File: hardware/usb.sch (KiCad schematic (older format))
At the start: 33 parts, among them J2 USB_B_Micro, U14 FT2232H, U31 93LCxxB, Y1 12MHz

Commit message: Improved documentation and parts of the schematic.
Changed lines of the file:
@@
 U 1 1 583B312F
 P 4400 3350
-F 0 "R80" V 4300 3350 50  0000 C CNN
-F 1 "0" V 4400 3350 50  0000 C CNN
+F 0 "R80" V 4193 3350 50  0000 C CNN
+F 1 "0" V 4284 3350 50  0000 C CNN
 F 2 "Resistor_SMD:R_0402_1005Metric" V 4330 3350 30  0001 C CNN
 F 3 "" H 4400 3350 30  0000 C CNN
@@
 U 1 1 583B315C
 P 4400 3450
-F 0 "R81" V 4480 3450 50  0000 C CNN
-F 1 "0" V 4400 3450 50  0000 C CNN
+F 0 "R81" V 4500 3450 50  0000 C CNN
+F 1 "0" V 4600 3450 50  0000 C CNN
 F 2 "Resistor_SMD:R_0402_1005Metric" V 4330 3450 30  0001 C CNN
 F 3 "" H 4400 3450 30  0000 C CNN
@@
 U 1 1 583B5C84
 P 8000 4150
-F 0 "R84" V 8080 4150 50  0000 C CNN
-F 1 "33" V 8000 4150 50  0000 C CNN
+F 0 "R84" V 7793 4150 50  0000 C CNN
+F 1 "33" V 7884 4150 50  0000 C CNN
 F 2 "Resistor_SMD:R_0402_1005Metric" V 7930 4150 30  0001 C CNN
 F 3 "" H 8000 4150 30  0000 C CNN
@@
 U 1 1 583B5CC5
 P 8400 4250
-F 0 "R88" V 8480 4250 50  0000 C CNN
-F 1 "33" V 8400 4250 50  0000 C CNN
+F 0 "R88" V 8200 4250 50  0000 C CNN
+F 1 "33" V 8300 4250 50  0000 C CNN
 F 2 "Resistor_SMD:R_0402_1005Metric" V 8330 4250 30  0001 C CNN
 F 3 "" H 8400 4250 30  0000 C CNN
@@
 U 1 1 583B63A8
 P 8000 4450
-F 0 "R85" V 8080 4450 50  0000 C CNN
-F 1 "33" V 8000 4450 50  0000 C CNN
+F 0 "R85" V 8115 4450 50  0000 C CNN
+F 1 "33" V 8206 4450 50  0000 C CNN
 F 2 "Resistor_SMD:R_0402_1005Metric" V 7930 4450 30  0001 C CNN
 F 3 "" H 8000 4450 30  0000 C CNN
@@
 U 1 1 596BF8E7
 P 4850 3850
-F 0 "R72" V 4930 3850 50  0000 C CNN
-F 1 "1k" V 4850 3850 50  0000 C CNN
+F 0 "R72" V 4965 3850 50  0000 C CNN
+F 1 "1k" V 5056 3850 50  0000 C CNN
 F 2 "Resistor_SMD:R_0402_1005Metric" V 4780 3850 30  0001 C CNN
 F 3 "" H 4850 3850 30  0000 C CNN

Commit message: Changed components to official libs.
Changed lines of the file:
@@
 U 1 1 596C00A3
 P 4250 3900
-F 0 "R71" V 4330 3900 50  0000 C CNN
-F 1 "12k" V 4250 3900 50  0000 C CNN
+F 0 "R71" H 4181 3946 50  0000 R CNN
+F 1 "12k" H 4181 3855 50  0000 R CNN
 F 2 "Resistor_SMD:R_0402_1005Metric" V 4180 3900 30  0001 C CNN
 F 3 "" H 4250 3900 30  0000 C CNN

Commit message: Finished design, began routing.
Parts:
- R26: renamed from R82; MFN ERJ-2GEJ472X -> ERJ-2GEJ472X
- Y1: footprint Crystal:Crystal_SMD_Abracon_ABM10-4Pin_2.5x2.0mm -> fmcw:ABM10; symbol Device:Crystal -> Device:Crystal_GND24
- renumbered C207 to C59, C208 to C60, C209 to C61, C152 to C62, C153 to C63, C154 to C64, C210 to C65, C155 to C66, C156 to C67, C157 to C68, C211 to C69, C212 to C70, C158 to C71, C159 to C72, C160 to C73, C161 to C74, FB14 to FB3, FB12 to FB4, R73 to R17, R79 to R18, R71 to R19, R80 to R20, R81 to R21, R72 to R22, R84 to R23, R85 to R24, R88 to R25, R83 to R27, U31 to U8, U14 to U9
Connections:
- wire segments 134 -> 139
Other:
- moved on the sheet: C62, C63, C64, R26

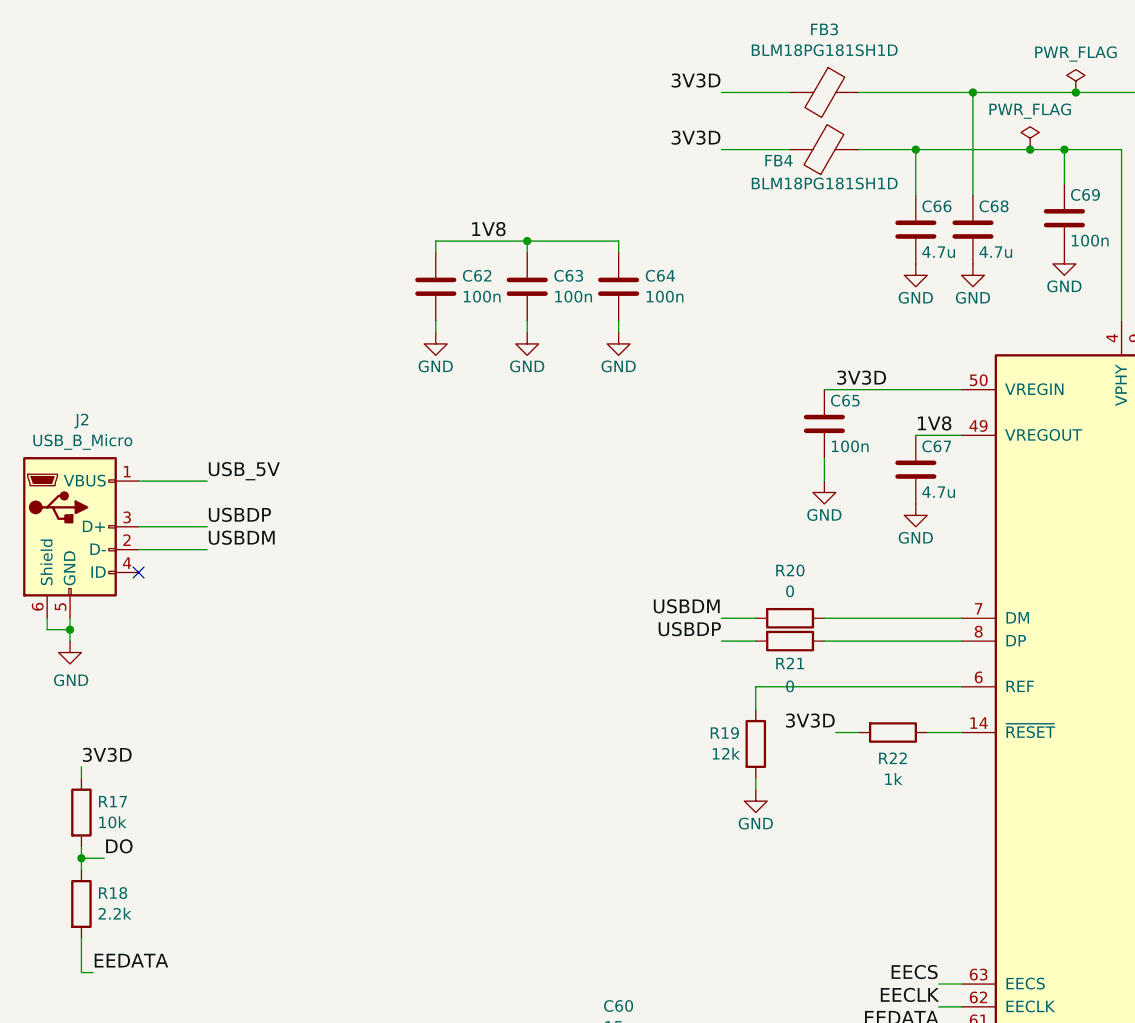
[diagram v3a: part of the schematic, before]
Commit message: Completed clock placement and routing.
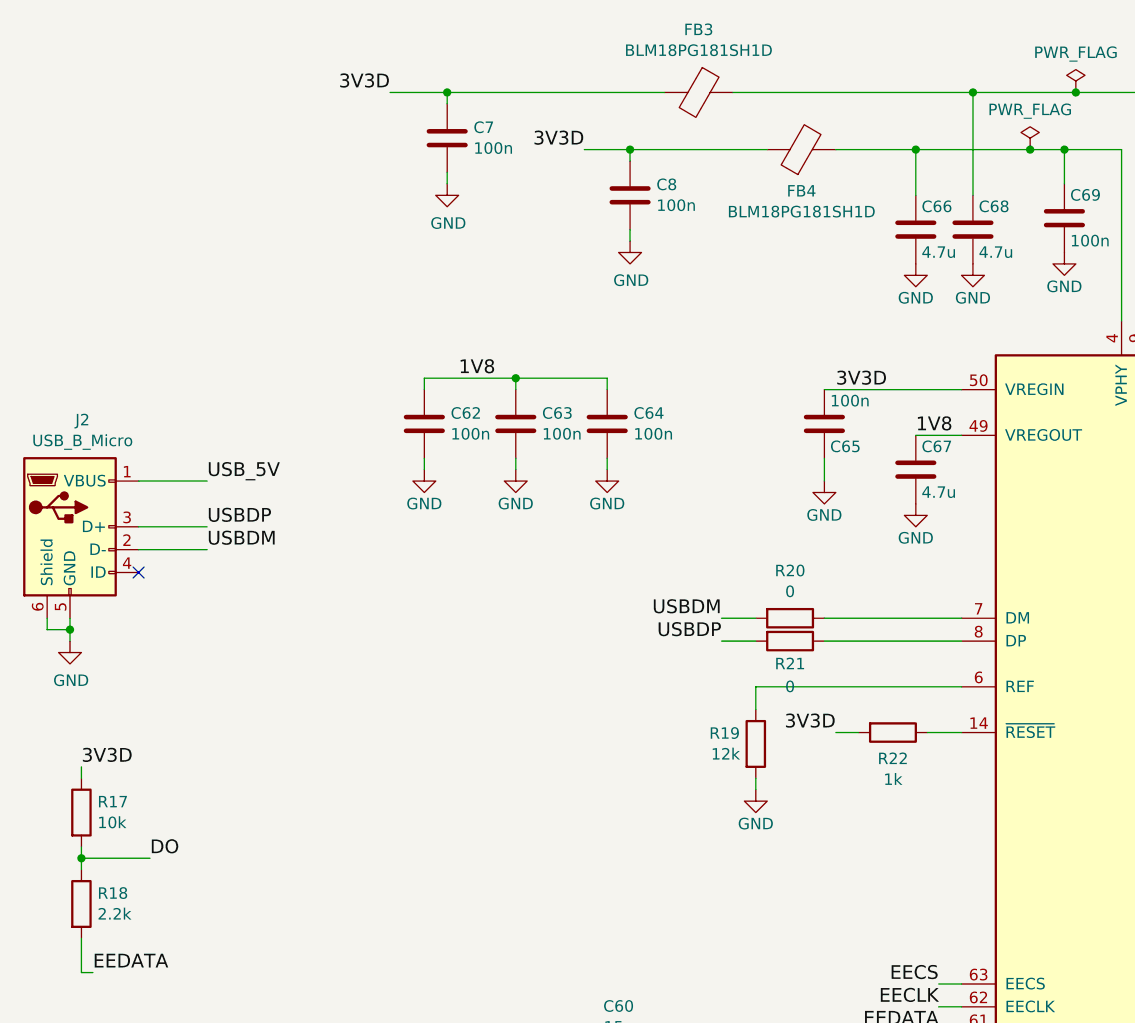
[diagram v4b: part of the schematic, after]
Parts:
- added C7, C8: 100n, Capacitor_SMD:C_0402_1005Metric, symbol Device:C
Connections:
- net 3V3D: now also C65.2, C7.1, C8.1; no longer C65.1
- net GND: now also C65.1, C7.2, C8.2; no longer C65.2
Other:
- moved on the sheet: C62, C63, C64, FB3, FB4
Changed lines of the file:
@@
 F 4 "CL05B104KO5NNNC" H 0   0   50  0001 C CNN "MFN"
 	1    4550 2500
-	1    0    0    -1
+	1    0    0    1
 $EndComp
 $Comp
@@
 	1    0    0    -1
 $EndComp
-Text Label 1400 4400 0    60   ~ 0
+Text Label 1600 4400 0    60   ~ 0
 DO
 Text Label 1350 4900 0    60   ~ 0
@@
 L Device:Ferrite_Bead FB4
 U 1 1 5865C0D7
-P 4550 1300
-F 0 "FB4" V 4500 1500 50  0000 C CNN
-F 1 "BLM18PG181SH1D" V 4400 1300 50  0000 C CNN
-F 2 "Inductor_SMD:L_0603_1608Metric" H 4550 1300 60  0001 C CNN
-F 3 "" H 4550 1300 60  0000 C CNN
-F 4 "BLM18PG181SH1D" H 0   0   50  0001 C CNN "MFN"
-	1    4550 1300
+P 4450 1300
+F 0 "FB4" V 4268 1300 50  0000 C CNN
+F 1 "BLM18PG181SH1D" V 4177 1300 50  0000 C CNN
+F 2 "Inductor_SMD:L_0603_1608Metric" H 4450 1300 60  0001 C CNN
+F 3 "" H 4450 1300 60  0000 C CNN
+F 4 "BLM18PG181SH1D" H -100 0   50  0001 C CNN "MFN"
+	1    4450 1300
 	0    -1   -1   0
 $EndComp
@@
 L Device:Ferrite_Bead FB3
 U 1 1 596BB650
-P 4550 1050
-F 0 "FB3" V 4276 1050 50  0000 C CNN
-F 1 "BLM18PG181SH1D" V 4367 1050 50  0000 C CNN
-F 2 "Inductor_SMD:L_0603_1608Metric" H 4550 1050 60  0001 C CNN
-F 3 "" H 4550 1050 60  0000 C CNN
-F 4 "BLM18PG181SH1D" H 0   0   50  0001 C CNN "MFN"
-	1    4550 1050
+P 4000 1050
+F 0 "FB3" V 3726 1050 50  0000 C CNN
+F 1 "BLM18PG181SH1D" V 3817 1050 50  0000 C CNN
+F 2 "Inductor_SMD:L_0603_1608Metric" H 4000 1050 60  0001 C CNN
+F 3 "" H 4000 1050 60  0000 C CNN
+F 4 "BLM18PG181SH1D" H -550 0   50  0001 C CNN "MFN"
+	1    4000 1050
 	0    1    1    0
 $EndComp
@@
 	1300 4900 1350 4900
 Wire Wire Line
-	1400 4400 1300 4400
+	1600 4400 1300 4400
 Connection ~ 1300 4400
 Wire Wire Line
@@
 	1    0    0    -1
 $EndComp
-Text Label 4100 1050 2    60   ~ 0
+Text Label 2650 1050 2    60   ~ 0
 3V3D
-Text Label 4100 1300 2    60   ~ 0
+Text Label 3500 1300 2    60   ~ 0
 3V3D
 $Comp
@@
 L Device:C C63
 U 1 1 596C4AA8
-P 3250 1900
-F 0 "C63" H 3365 1946 50  0000 L CNN
-F 1 "100n" H 3365 1855 50  0000 L CNN
-F 2 "Capacitor_SMD:C_0402_1005Metric" H 3288 1750 30  0001 C CNN
-F 3 "" H 3250 1900 60  0000 C CNN
-F 4 "CL05B104KO5NNNC" H -700 0   50  0001 C CNN "MFN"
-	1    3250 1900
+P 3200 2500
+F 0 "C63" H 3315 2546 50  0000 L CNN
+F 1 "100n" H 3315 2455 50  0000 L CNN
+F 2 "Capacitor_SMD:C_0402_1005Metric" H 3238 2350 30  0001 C CNN
+F 3 "" H 3200 2500 60  0000 C CNN
+F 4 "CL05B104KO5NNNC" H -750 600 50  0001 C CNN "MFN"
+	1    3200 2500
 	1    0    0    -1
 $EndComp
@@
 L Device:C C64
 U 1 1 596C4AFE
-P 3650 1900
-F 0 "C64" H 3765 1946 50  0000 L CNN
-F 1 "100n" H 3765 1855 50  0000 L CNN
-F 2 "Capacitor_SMD:C_0402_1005Metric" H 3688 1750 30  0001 C CNN
-F 3 "" H 3650 1900 60  0000 C CNN
-F 4 "CL05B104KO5NNNC" H -500 0   50  0001 C CNN "MFN"
-	1    3650 1900
+P 3600 2500
+F 0 "C64" H 3715 2546 50  0000 L CNN
+F 1 "100n" H 3715 2455 50  0000 L CNN
+F 2 "Capacitor_SMD:C_0402_1005Metric" H 3638 2350 30  0001 C CNN
+F 3 "" H 3600 2500 60  0000 C CNN
+F 4 "CL05B104KO5NNNC" H -550 600 50  0001 C CNN "MFN"
+	1    3600 2500
 	1    0    0    -1
 $EndComp
@@
 L power:GND #PWR055
 U 1 1 596C4CA2
-P 3650 2100
-F 0 "#PWR055" H 3650 1850 50  0001 C CNN
-F 1 "GND" H 3650 1950 50  0000 C CNN
-F 2 "" H 3650 2100 60  0000 C CNN
-F 3 "" H 3650 2100 60  0000 C CNN
-	1    3650 2100
+P 3600 2700
+F 0 "#PWR055" H 3600 2450 50  0001 C CNN
+F 1 "GND" H 3600 2550 50  0000 C CNN
+F 2 "" H 3600 2700 60  0000 C CNN
+F 3 "" H 3600 2700 60  0000 C CNN
+	1    3600 2700
 	1    0    0    -1
 $EndComp
@@
 L power:GND #PWR054
 U 1 1 596C4CF6
-P 3250 2100
-F 0 "#PWR054" H 3250 1850 50  0001 C CNN
-F 1 "GND" H 3250 1950 50  0000 C CNN
-F 2 "" H 3250 2100 60  0000 C CNN
-F 3 "" H 3250 2100 60  0000 C CNN
-	1    3250 2100
+P 3200 2700
+F 0 "#PWR054" H 3200 2450 50  0001 C CNN
+F 1 "GND" H 3200 2550 50  0000 C CNN
+F 2 "" H 3200 2700 60  0000 C CNN
+F 3 "" H 3200 2700 60  0000 C CNN
+	1    3200 2700
 	1    0    0    -1
 $EndComp
@@
 L power:GND #PWR053
 U 1 1 596C4D43
-P 2850 2100
-F 0 "#PWR053" H 2850 1850 50  0001 C CNN
-F 1 "GND" H 2850 1950 50  0000 C CNN
-F 2 "" H 2850 2100 60  0000 C CNN
-F 3 "" H 2850 2100 60  0000 C CNN
-	1    2850 2100
-	1    0    0    -1
-$EndComp
-Wire Wire Line
-	3250 1700 3250 1750
-Wire Wire Line
-	3650 1700 3650 1750
-Text Label 3000 1700 0    60   ~ 0
+P 2800 2700
+F 0 "#PWR053" H 2800 2450 50  0001 C CNN
+F 1 "GND" H 2800 2550 50  0000 C CNN
+F 2 "" H 2800 2700 60  0000 C CNN
+F 3 "" H 2800 2700 60  0000 C CNN
+	1    2800 2700
+	1    0    0    -1
+$EndComp
+Wire Wire Line
+	3200 2300 3200 2350
+Wire Wire Line
+	3600 2300 3600 2350
+Text Label 2950 2300 0    60   ~ 0
 1V8
 Wire Wire Line
@@
 	6250 1950 6350 1950
 Wire Wire Line
-	3250 1700 3650 1700
+	3200 2300 3600 2300
 $Comp
 L Interface_USB:FT2232H U9
@@
 $EndComp
 Wire Wire Line
-	4700 1300 4950 1300
-Wire Wire Line
-	4100 1300 4400 1300
-Wire Wire Line
-	4100 1050 4400 1050
-Wire Wire Line
-	4700 1050 5200 1050
+	4600 1300 4950 1300
+Wire Wire Line
+	2650 1050 2900 1050
+Wire Wire Line
+	4150 1050 5200 1050
 Wire Wire Line
 	8600 5300 8600 5400
@@
 	6650 1050 7150 1050
 Wire Wire Line
-	2850 2100 2850 2050
+	2800 2700 2800 2650
 $Comp
 L Device:C C62
 U 1 1 596C4A23
-P 2850 1900
-F 0 "C62" H 2965 1946 50  0000 L CNN
-F 1 "100n" H 2965 1855 50  0000 L CNN
-F 2 "Capacitor_SMD:C_0402_1005Metric" H 2888 1750 30  0001 C CNN
-F 3 "" H 2850 1900 60  0000 C CNN
-F 4 "CL05B104KO5NNNC" H -900 0   50  0001 C CNN "MFN"
-	1    2850 1900
-	1    0    0    -1
-$EndComp
-Connection ~ 3250 1700
-Wire Wire Line
-	2850 1700 2850 1750
-Wire Wire Line
-	2850 1700 3250 1700
-Wire Wire Line
-	3250 2100 3250 2050
-Wire Wire Line
-	3650 2100 3650 2050
+P 2800 2500
+F 0 "C62" H 2915 2546 50  0000 L CNN
+F 1 "100n" H 2915 2455 50  0000 L CNN
+F 2 "Capacitor_SMD:C_0402_1005Metric" H 2838 2350 30  0001 C CNN
+F 3 "" H 2800 2500 60  0000 C CNN
+F 4 "CL05B104KO5NNNC" H -950 600 50  0001 C CNN "MFN"
+	1    2800 2500
+	1    0    0    -1
+$EndComp
+Connection ~ 3200 2300
+Wire Wire Line
+	2800 2300 2800 2350
+Wire Wire Line
+	2800 2300 3200 2300
+Wire Wire Line
+	3200 2700 3200 2650
+Wire Wire Line
+	3600 2700 3600 2650
 Wire Wire Line
 	4250 4100 4250 4050
@@
 NoConn ~ 3600 5650
 NoConn ~ 4000 5650
+$Comp
+L Device:C C8
+U 1 1 5C794EE9
+P 3700 1500
+F 0 "C8" H 3815 1546 50  0000 L CNN
+F 1 "100n" H 3815 1455 50  0000 L CNN
+F 2 "Capacitor_SMD:C_0402_1005Metric" H 3738 1350 30  0001 C CNN
+F 3 "" H 3700 1500 60  0000 C CNN
+F 4 "CL05B104KO5NNNC" H -1900 -100 50  0001 C CNN "MFN"
+	1    3700 1500
+	1    0    0    -1
+$EndComp
+Wire Wire Line
+	3500 1300 3700 1300
+$Comp
+L Device:C C7
+U 1 1 5C7A4A00
+P 2900 1250
+F 0 "C7" H 3015 1296 50  0000 L CNN
+F 1 "100n" H 3015 1205 50  0000 L CNN
+F 2 "Capacitor_SMD:C_0402_1005Metric" H 2938 1100 30  0001 C CNN
+F 3 "" H 2900 1250 60  0000 C CNN
+F 4 "CL05B104KO5NNNC" H -2700 -350 50  0001 C CNN "MFN"
+	1    2900 1250
+	1    0    0    -1
+$EndComp
+$Comp
+L power:GND #PWR011
+U 1 1 5C7A52FB
+P 2900 1450
+F 0 "#PWR011" H 2900 1200 50  0001 C CNN
+F 1 "GND" H 2905 1277 50  0000 C CNN
+F 2 "" H 2900 1450 50  0001 C CNN
+F 3 "" H 2900 1450 50  0001 C CNN
+	1    2900 1450
+	1    0    0    -1
+$EndComp
+Wire Wire Line
+	2900 1450 2900 1400
+Wire Wire Line
+	2900 1050 2900 1100
+Connection ~ 2900 1050
+Wire Wire Line
+	2900 1050 3850 1050
+Wire Wire Line
+	3700 1350 3700 1300
+Connection ~ 3700 1300
+Wire Wire Line
+	3700 1300 4300 1300
+$Comp
+L power:GND #PWR079
+U 1 1 5C7B858F
+P 3700 1700
+F 0 "#PWR079" H 3700 1450 50  0001 C CNN
+F 1 "GND" H 3705 1527 50  0000 C CNN
+F 2 "" H 3700 1700 50  0001 C CNN
+F 3 "" H 3700 1700 50  0001 C CNN
+	1    3700 1700
+	1    0    0    -1
+$EndComp
+Wire Wire Line
+	3700 1700 3700 1650
 $EndSCHEMATC

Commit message: Improve PCB.
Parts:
- removed U8: 93LCxxB, Package_SO:SOIC-8_3.9x4.9mm_P1.27mm, symbol Memory_EEPROM:93LCxxB
- added R3, R82: 10k, Resistor_SMD:R_0402_1005Metric, symbol Device:R
- added U8: 93LCxxBxxOT, Package_TO_SOT_SMD:SOT-23-6, symbol Memory_EEPROM:93LCxxBxxOT
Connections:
- net 3V3D: now also R3.1, R82.1, U8.6 (VCC)
- net DO: now also U8.1 (DO)
- net EECLK: now also R3.2, U8.4 (CLK)
- net EECS: now also R82.2, U8.5 (CS)
- net EEDATA: now also U8.3 (DI)
- net GND: now also U8.2 (GND)
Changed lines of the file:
@@
 Title "FMCW"
 Date ""
-Rev "v2.0"
+Rev "v2.0c"
 Comp ""
 Comment1 ""
@@
 	1    0    0    -1
 $EndComp
-Text Label 2950 6950 2    60   ~ 0
+Text Label 2950 7050 2    60   ~ 0
 EECS
 Text Label 4000 6950 0    60   ~ 0
@@
 	1300 4350 1300 4400
 Wire Wire Line
-	2950 6950 3100 6950
+	2950 7050 3100 7050
 Wire Wire Line
 	4000 6950 3900 6950
@@
 	5100 6050 5100 6550
 Wire Wire Line
-	5150 4950 5050 4950
-Wire Wire Line
-	5150 5050 5050 5050
+	5150 4950 4950 4950
+Wire Wire Line
+	5150 5050 4300 5050
 Wire Wire Line
 	5150 5150 5050 5150
-Text Label 5050 4950 2    60   ~ 0
+Text Label 4800 4950 2    60   ~ 0
 EECS
-Text Label 5050 5050 2    60   ~ 0
+Text Label 4150 5050 2    60   ~ 0
 EECLK
 Text Label 5050 5150 2    60   ~ 0
@@
 Wire Wire Line
 	7550 5750 8600 5750
-$Comp
-L Memory_EEPROM:93LCxxB U8
-U 1 1 6321F24D
-P 3500 7050
-F 0 "U8" H 3750 6800 50  0000 C CNN
-F 1 "93LCxxB" H 3700 7300 50  0000 C CNN
-F 2 "Package_SO:SOIC-8_3.9x4.9mm_P1.27mm" H 3500 7050 50  0001 C CNN
-F 3 "http://ww1.microchip.com/downloads/en/DeviceDoc/20001749K.pdf" H 3500 7050 50  0001 C CNN
-F 4 "93LC46BT-I/SN" H 3500 7050 50  0001 C CNN "MFN"
-	1    3500 7050
-	1    0    0    -1
-$EndComp
 Wire Wire Line
 	3500 6750 3500 6450
@@
 Wire Wire Line
 	3700 1700 3700 1650
+$Comp
+L Device:R R82
+U 1 1 5C8A2FB6
+P 4950 4750
+F 0 "R82" H 5020 4796 50  0000 L CNN
+F 1 "10k" H 5020 4705 50  0000 L CNN
+F 2 "Resistor_SMD:R_0402_1005Metric" V 4880 4750 30  0001 C CNN
+F 3 "" H 4950 4750 30  0000 C CNN
+F 4 "ERJ-2RKF1002X" H 3650 550 50  0001 C CNN "MFN"
+	1    4950 4750
+	1    0    0    -1
+$EndComp
+Wire Wire Line
+	4950 4600 4950 4550
+Text Label 4950 4550 0    60   ~ 0
+3V3D
+Wire Wire Line
+	4950 4900 4950 4950
+Connection ~ 4950 4950
+Wire Wire Line
+	4950 4950 4800 4950
+$Comp
+L Device:R R3
+U 1 1 5C8AFF9B
+P 4300 4850
+F 0 "R3" H 4370 4896 50  0000 L CNN
+F 1 "10k" H 4370 4805 50  0000 L CNN
+F 2 "Resistor_SMD:R_0402_1005Metric" V 4230 4850 30  0001 C CNN
+F 3 "" H 4300 4850 30  0000 C CNN
+F 4 "ERJ-2RKF1002X" H 3000 650 50  0001 C CNN "MFN"
+	1    4300 4850
+	1    0    0    -1
+$EndComp
+Wire Wire Line
+	4300 5000 4300 5050
+Connection ~ 4300 5050
+Wire Wire Line
+	4300 5050 4150 5050
+Wire Wire Line
+	4300 4700 4300 4650
+Text Label 4300 4650 0    60   ~ 0
+3V3D
+$Comp
+L Memory_EEPROM:93LCxxBxxOT U8
+U 1 1 5C920D7F
+P 3500 7050
+F 0 "U8" H 3250 7300 50  0000 C CNN
+F 1 "93LCxxBxxOT" H 3800 6800 50  0000 C CNN
+F 2 "Package_TO_SOT_SMD:SOT-23-6" H 3500 7050 50  0001 C CNN
+F 3 "http://ww1.microchip.com/downloads/en/DeviceDoc/20001749K.pdf" H 3500 7050 50  0001 C CNN
+F 4 "93LC46BT-I/OT" H 3500 7050 50  0001 C CNN "MFN"
+	1    3500 7050
+	1    0    0    -1
+$EndComp
 $EndSCHEMATC
